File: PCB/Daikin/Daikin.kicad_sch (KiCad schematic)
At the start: 19 parts, among them J1 1x4, J2 Prog, Q3 PMF250XNEX, U1 ESP32-PICO-MINI-02, U2 LMR16006YDDCR

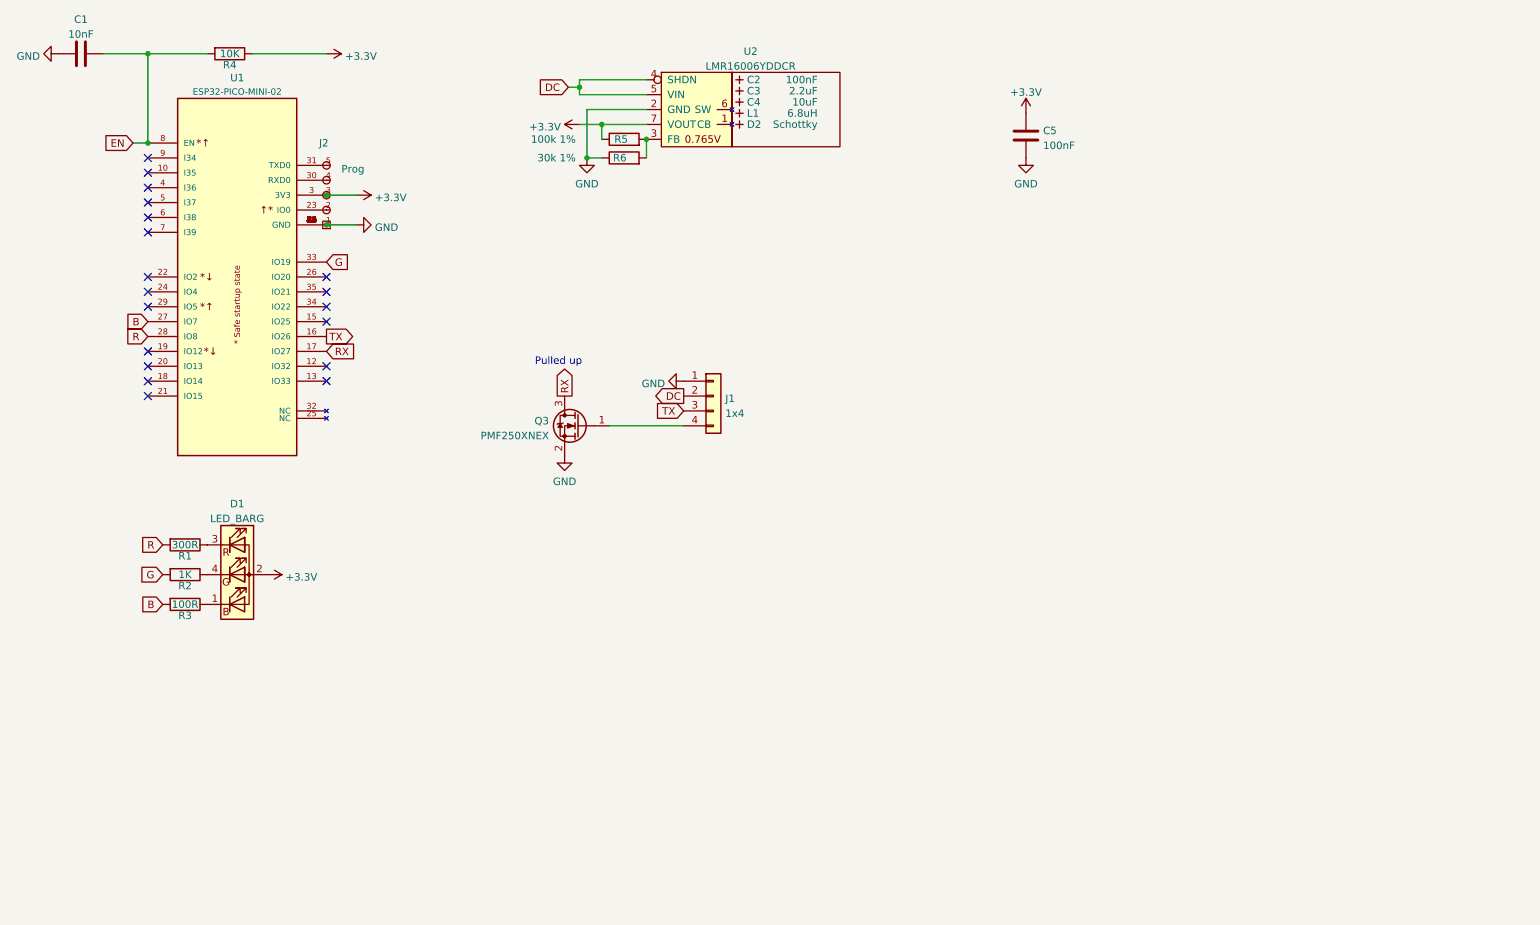
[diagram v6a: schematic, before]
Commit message: Changed PCB - larger so under pins making harder to fit plug the wrong way. Also changed to 5 pin connector to natch the actual plug to avoid confusion.
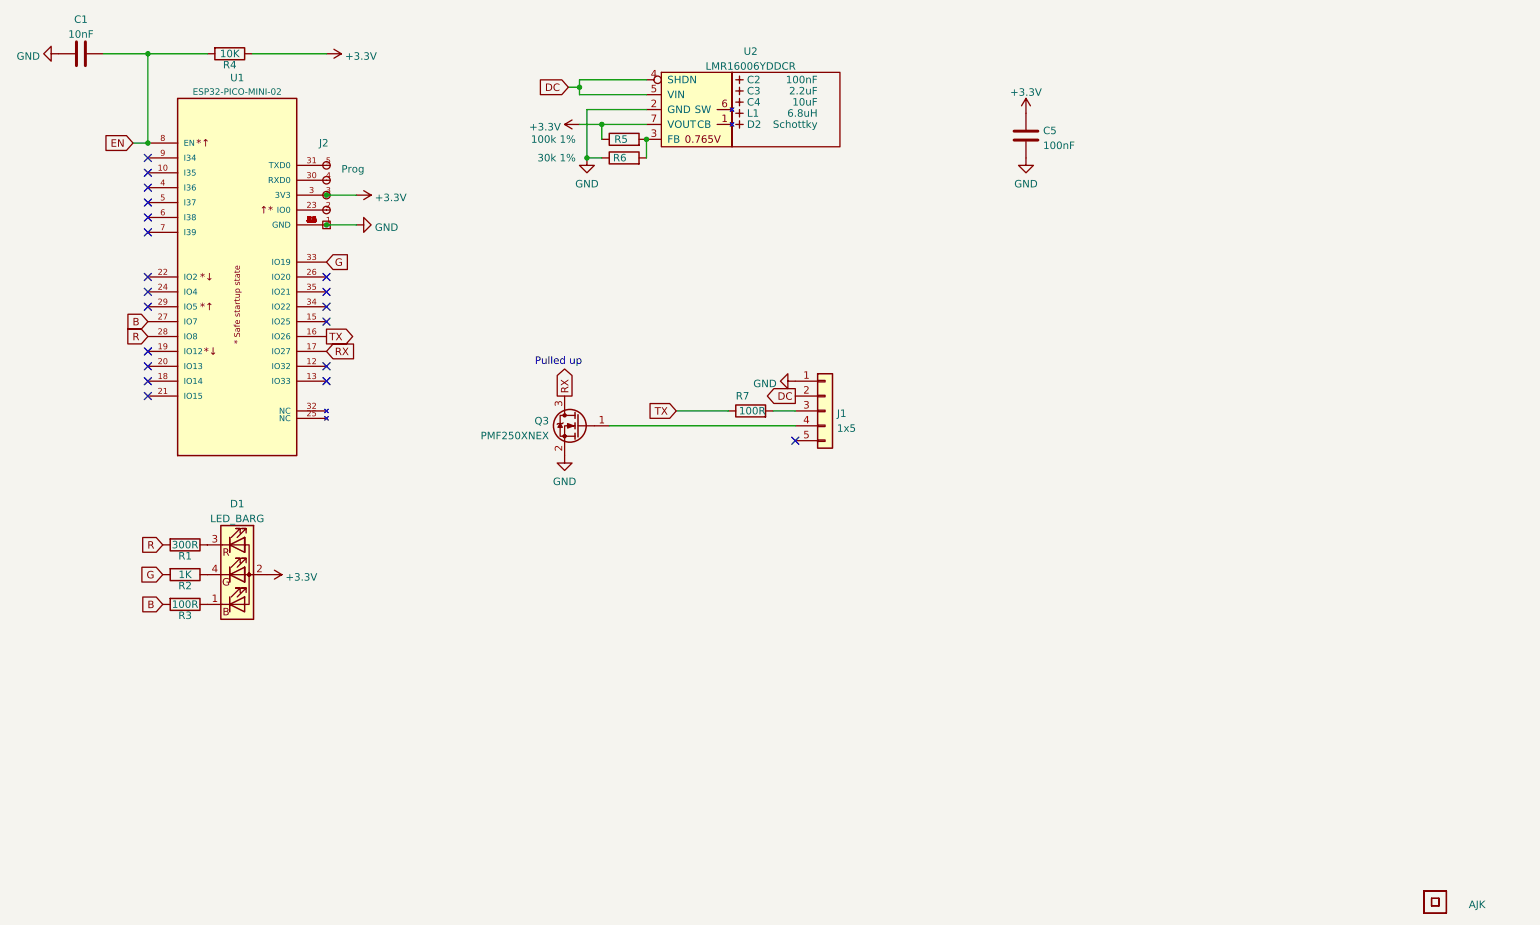
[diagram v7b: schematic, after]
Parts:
- added Logo1: AJK, RevK:AJK, symbol RevK:AJK
- added R7: 100R, RevK:R_0603, symbol Device:R
- added U3: QR, RevK:QR-DAIKIN, symbol RevK:QR
- J1: value 1x4 -> 1x5; footprint RevK:JLC-PinHeader_1x04_P2.54mm_Right -> RevK:PinHeader_1x05_P2.54mm_Right; symbol Connector_Generic:Conn_01x04 -> Connector_Generic:Conn_01x05; LCSC Part # C91552 -> C225491
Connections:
- net TX: now also R7.1; no longer J1.3 (Pin_3)
- new net: J1.3 (Pin_3), R7.2
- no-connect marks 19 -> 20
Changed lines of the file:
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@@
   (junction (at 81.28 57.15) (diameter 0) (color 0 0 0 0)
   )
+  (no_connect (at 161.29 93.98))
   (no_connect (at 81.28 71.12))
   (no_connect (at 50.8 45.72))
@@
     (stroke (width 0) (type default) (color 0 0 0 0))
   )
-  (wire (pts (xy 142.24 91.44) (xy 129.54 91.44))
+  (wire (pts (xy 161.29 91.44) (xy 129.54 91.44))
     (stroke (width 0) (type default) (color 0 0 0 0))
   )
@@
     (stroke (width 0) (type default) (color 0 0 0 0))
   )
+  (wire (pts (xy 140.97 88.9) (xy 149.86 88.9))
+    (stroke (width 0) (type default) (color 0 0 0 0))
+  )
   (wire (pts (xy 128.27 40.005) (xy 135.89 40.005))
     (stroke (width 0) (type default) (color 0 0 0 0))
@@
   )
   (wire (pts (xy 124.46 32.385) (xy 135.89 32.385))
+    (stroke (width 0) (type default) (color 0 0 0 0))
+  )
+  (wire (pts (xy 157.48 88.9) (xy 161.29 88.9))
     (stroke (width 0) (type default) (color 0 0 0 0))
   )
@@
     )
   )
-  (global_label "TX" (shape input) (at 142.24 88.9 180) (fields_autoplaced)
+  (global_label "TX" (shape input) (at 140.97 88.9 180) (fields_autoplaced)
     (effects (font (size 1.27 1.27)) (justify right))
-    (property "Intersheet References" "${INTERSHEET_REFS}" (id 0) (at 137.7387 88.8206 0)
+    (property "Intersheet References" "${INTERSHEET_REFS}" (id 0) (at 136.4687 88.8206 0)
       (effects (font (size 1.27 1.27)) (justify right) hide)
     )
@@
     )
   )
-  (global_label "DC" (shape output) (at 142.24 86.36 180) (fields_autoplaced)
+  (global_label "DC" (shape output) (at 161.29 86.36 180) (fields_autoplaced)
     (effects (font (size 1.27 1.27)) (justify right))
-    (property "Intersheet References" "${INTERSHEET_REFS}" (id 0) (at 137.3758 86.2806 0)
+    (property "Intersheet References" "${INTERSHEET_REFS}" (id 0) (at 156.4258 86.2806 0)
       (effects (font (size 1.27 1.27)) (justify right) hide)
     )
@@
     (pin "7")
   )
-  (symbol (lib_id "power:GND") (at 142.24 83.82 270) (unit 1)
-    (in_bom yes) (on_board yes) (fields_autoplaced)
-    (property "Reference" "#PWR09" (id 0) (at 135.89 83.82 0)
-      (effects (font (size 1.27 1.27)) hide)
-    )
-    (property "Value" "GND" (id 1) (at 139.0651 84.2538 90)
+  (symbol (lib_id "power:GND") (at 161.29 83.82 270) (unit 1)
+    (in_bom yes) (on_board yes) (fields_autoplaced)
+    (property "Reference" "#PWR09" (id 0) (at 154.94 83.82 0)
+      (effects (font (size 1.27 1.27)) hide)
+    )
+    (property "Value" "GND" (id 1) (at 158.1151 84.2538 90)
       (effects (font (size 1.27 1.27)) (justify right))
     )
-    (property "Footprint" "" (id 2) (at 142.24 83.82 0)
-      (effects (font (size 1.27 1.27)) hide)
-    )
-    (property "Datasheet" "" (id 3) (at 142.24 83.82 0)
+    (property "Footprint" "" (id 2) (at 161.29 83.82 0)
+      (effects (font (size 1.27 1.27)) hide)
+    )
+    (property "Datasheet" "" (id 3) (at 161.29 83.82 0)
       (effects (font (size 1.27 1.27)) hide)
     )
@@
     (pin "~")
   )
+  (symbol (lib_id "Device:R") (at 153.67 88.9 90) (unit 1)
+    (in_bom yes) (on_board yes)
+    (property "Reference" "R7" (id 0) (at 151.13 86.36 90)
+      (effects (font (size 1.27 1.27)) (justify right))
+    )
+    (property "Value" "100R" (id 1) (at 156.21 88.9 90)
+      (effects (font (size 1.27 1.27)) (justify left))
+    )
+    (property "Footprint" "RevK:R_0603" (id 2) (at 153.67 90.678 90)
+      (effects (font (size 1.27 1.27)) hide)
+    )
+    (property "Datasheet" "~" (id 3) (at 153.67 88.9 0)
+      (effects (font (size 1.27 1.27)) hide)
+    )
+    (property "LCSC Part #" "C105588" (id 4) (at 153.67 88.9 90)
+      (effects (font (size 1.27 1.27)) hide)
+    )
+    (pin "1")
+    (pin "2")
+  )
   (symbol (lib_id "Device:LED_BARG") (at 66.04 116.84 0) (unit 1)
     (in_bom yes) (on_board yes) (fields_autoplaced)
@@
     (pin "2")
   )
-  (symbol (lib_id "Connector_Generic:Conn_01x04") (at 147.32 86.36 0) (unit 1)
-    (in_bom yes) (on_board yes) (fields_autoplaced)
-    (property "Reference" "J1" (id 0) (at 149.352 86.7953 0)
-      (effects (font (size 1.27 1.27)) (justify left))
-    )
-    (property "Value" "1x4" (id 1) (at 149.352 89.3322 0)
-      (effects (font (size 1.27 1.27)) (justify left))
-    )
-    (property "Footprint" "RevK:JLC-PinHeader_1x04_P2.54mm_Right" (id 2) (at 148.59 93.98 0)
-      (effects (font (size 1.27 1.27)) hide)
-    )
-    (property "Datasheet" "~" (id 3) (at 147.32 86.36 0)
-      (effects (font (size 1.27 1.27)) hide)
-    )
-    (property "LCSC Part #" "C91552" (id 4) (at 147.32 86.36 0)
+  (symbol (lib_id "Connector_Generic:Conn_01x05") (at 166.37 88.9 0) (unit 1)
+    (in_bom yes) (on_board yes) (fields_autoplaced)
+    (property "Reference" "J1" (id 0) (at 168.402 89.3353 0)
+      (effects (font (size 1.27 1.27)) (justify left))
+    )
+    (property "Value" "1x5" (id 1) (at 168.402 91.8722 0)
+      (effects (font (size 1.27 1.27)) (justify left))
+    )
+    (property "Footprint" "RevK:PinHeader_1x05_P2.54mm_Right" (id 2) (at 166.37 88.9 0)
+      (effects (font (size 1.27 1.27)) hide)
+    )
+    (property "Datasheet" "~" (id 3) (at 166.37 88.9 0)
+      (effects (font (size 1.27 1.27)) hide)
+    )
+    (property "LCSC Part #" "C225491" (id 4) (at 166.37 88.9 0)
       (effects (font (size 1.27 1.27)) hide)
     )
@@
     (pin "3")
     (pin "4")
+    (pin "5")
   )
   (symbol (lib_id "power:+3.3V") (at 71.12 116.84 270) (unit 1)
@@
     (pin "1")
   )
+  (symbol (lib_id "RevK:QR") (at 270.51 172.72 0) (unit 1)
+    (in_bom no) (on_board yes) (fields_autoplaced)
+    (property "Reference" "U3" (id 0) (at 270.51 175.895 0)
+      (effects (font (size 1.27 1.27)) hide)
+    )
+    (property "Value" "QR" (id 1) (at 270.51 175.895 0)
+      (effects (font (size 1.27 1.27)) hide)
+    )
+    (property "Footprint" "RevK:QR-DAIKIN" (id 2) (at 269.875 173.355 0)
+      (effects (font (size 1.27 1.27)) hide)
+    )
+    (property "Datasheet" "" (id 3) (at 269.875 173.355 0)
+      (effects (font (size 1.27 1.27)) hide)
+    )
+    (property "Note" "Non part, PCB printed" (id 4) (at 270.51 172.72 0)
+      (effects (font (size 1.27 1.27)) hide)
+    )
+  )
   (symbol (lib_id "Device:R") (at 132.08 42.545 90) (unit 1)
     (in_bom yes) (on_board yes)
@@
     (pin "5")
   )
+  (symbol (lib_id "RevK:AJK") (at 275.59 172.72 0) (unit 1)
+    (in_bom no) (on_board yes) (fields_autoplaced)
+    (property "Reference" "Logo1" (id 0) (at 275.59 170.18 0)
+      (effects (font (size 1.27 1.27)) hide)
+    )
+    (property "Value" "AJK" (id 1) (at 276.225 173.1538 0)
+      (effects (font (size 1.27 1.27)) (justify left))
+    )
+    (property "Footprint" "RevK:AJK" (id 2) (at 275.59 175.26 0)
+      (effects (font (size 1.27 1.27)) hide)
+    )
+    (property "Datasheet" "" (id 3) (at 275.59 175.26 0)
+      (effects (font (size 1.27 1.27)) hide)
+    )
+    (property "Note" "Non part, PCB printed" (id 4) (at 275.59 172.72 0)
+      (effects (font (size 1.27 1.27)) hide)
+    )
+  )
   (sheet_instances
     (path "/" (page "1"))
@@
     )
     (path "/af073fa6-a783-40f2-9751-692984a62ffc"
-      (reference "J1") (unit 1) (value "1x4") (footprint "RevK:JLC-PinHeader_1x04_P2.54mm_Right")
+      (reference "J1") (unit 1) (value "1x5") (footprint "RevK:PinHeader_1x05_P2.54mm_Right")
     )
     (path "/ee567585-ddb7-4c4a-a692-94261f4c4bce"
@@
       (reference "L1") (unit 1) (value "6.8uH") (footprint "RevK:L_4x4_")
     )
+    (path "/f93331c2-c430-4421-8c6c-fa9ccbf3197e"
+      (reference "Logo1") (unit 1) (value "AJK") (footprint "RevK:AJK")
+    )
     (path "/ebcfdf36-110d-4f79-9de0-e4fcd76c1d6e"
       (reference "Q3") (unit 1) (value "PMF250XNEX") (footprint "RevK:SOT-323_SC-70")
@@
       (reference "R6") (unit 1) (value "30k 1%") (footprint "RevK:R_0603")
     )
+    (path "/a10dd132-8952-4c17-b7c1-5ab3a5e86621"
+      (reference "R7") (unit 1) (value "100R") (footprint "RevK:R_0603")
+    )
     (path "/7943a3d5-b195-4a57-b3e1-ee29355f1eeb"
       (reference "U1") (unit 1) (value "ESP32-PICO-MINI-02") (footprint "RevK:ESP32-PICO-MINI-02")
@@
       (reference "U2") (unit 1) (value "LMR16006YDDCR") (footprint "RevK:SOT-23-Thin-6-Reg")
     )
-  )
+    (path "/dd024a75-cbfd-4a06-88fc-e180db89ebee"
+      (reference "U3") (unit 1) (value "QR") (footprint "RevK:QR-DAIKIN")
+    )
+  )

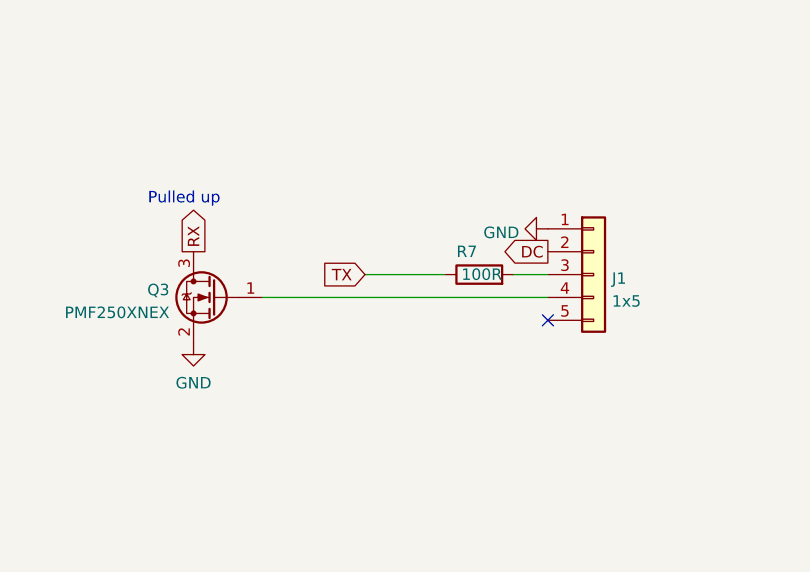
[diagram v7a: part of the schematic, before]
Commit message: Added some caps to I/O
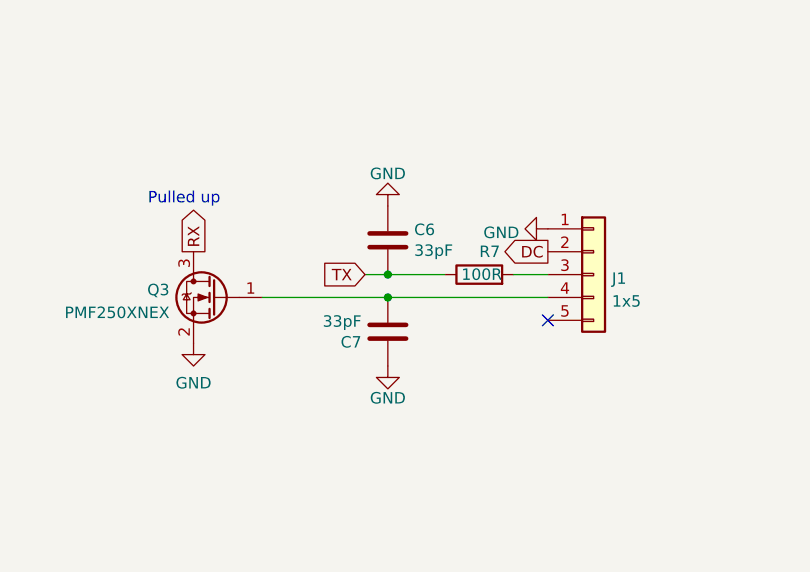
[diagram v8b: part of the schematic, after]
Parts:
- added C6, C7: 33pF, RevK:C_0603, symbol Device:C
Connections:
- net GND: now also C6.1, C7.1
- net TX: now also C6.2
- net at J1.4 (Pin_4), Q3.1 (G): now also C7.2
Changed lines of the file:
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@@
   (junction (at 128.27 40.005) (diameter 0) (color 0 0 0 0)
   )
+  (junction (at 143.51 91.44) (diameter 0) (color 0 0 0 0)
+  )
   (junction (at 81.28 52.07) (diameter 0) (color 0 0 0 0)
   )
   (junction (at 81.28 57.15) (diameter 0) (color 0 0 0 0)
+  )
+  (junction (at 143.51 88.9) (diameter 0) (color 0 0 0 0)
   )
   (no_connect (at 161.29 93.98))
@@
     (stroke (width 0) (type default) (color 0 0 0 0))
   )
-  (wire (pts (xy 161.29 91.44) (xy 129.54 91.44))
+  (wire (pts (xy 161.29 91.44) (xy 143.51 91.44))
     (stroke (width 0) (type default) (color 0 0 0 0))
   )
@@
     (stroke (width 0) (type default) (color 0 0 0 0))
   )
-  (wire (pts (xy 140.97 88.9) (xy 149.86 88.9))
+  (wire (pts (xy 140.97 88.9) (xy 143.51 88.9))
     (stroke (width 0) (type default) (color 0 0 0 0))
   )
@@
     (stroke (width 0) (type default) (color 0 0 0 0))
   )
+  (wire (pts (xy 143.51 91.44) (xy 129.54 91.44))
+    (stroke (width 0) (type default) (color 0 0 0 0))
+  )
   (wire (pts (xy 128.27 45.72) (xy 125.73 45.72))
     (stroke (width 0) (type default) (color 0 0 0 0))
@@
   )
   (wire (pts (xy 124.46 40.005) (xy 128.27 40.005))
+    (stroke (width 0) (type default) (color 0 0 0 0))
+  )
+  (wire (pts (xy 143.51 88.9) (xy 149.86 88.9))
     (stroke (width 0) (type default) (color 0 0 0 0))
   )
@@
     )
     (property "Part No" "0603-680R" (id 4) (at 57.15 111.76 90)
+      (effects (font (size 1.27 1.27)) hide)
+    )
+    (pin "1")
+    (pin "2")
+  )
+  (symbol (lib_id "Device:C") (at 143.51 95.25 180) (unit 1)
+    (in_bom yes) (on_board yes)
+    (property "Reference" "C7" (id 0) (at 140.589 96.4184 0)
+      (effects (font (size 1.27 1.27)) (justify left))
+    )
+    (property "Value" "33pF" (id 1) (at 140.589 94.107 0)
+      (effects (font (size 1.27 1.27)) (justify left))
+    )
+    (property "Footprint" "RevK:C_0603" (id 2) (at 142.5448 91.44 0)
+      (effects (font (size 1.27 1.27)) hide)
+    )
+    (property "Datasheet" "" (id 3) (at 143.51 95.25 0)
+      (effects (font (size 1.27 1.27)) hide)
+    )
+    (property "Note" "" (id 4) (at 143.51 95.25 0)
+      (effects (font (size 1.27 1.27)) hide)
+    )
+    (property "Part No" "0603-33pF-50V" (id 5) (at 143.51 95.25 0)
+      (effects (font (size 1.27 1.27)) hide)
+    )
+    (property "Manufacturer" "" (id 6) (at 143.51 95.25 0)
       (effects (font (size 1.27 1.27)) hide)
     )
@@
     (pin "~")
   )
+  (symbol (lib_id "Device:C") (at 143.51 85.09 0) (unit 1)
+    (in_bom yes) (on_board yes)
+    (property "Reference" "C6" (id 0) (at 146.431 83.9216 0)
+      (effects (font (size 1.27 1.27)) (justify left))
+    )
+    (property "Value" "33pF" (id 1) (at 146.431 86.233 0)
+      (effects (font (size 1.27 1.27)) (justify left))
+    )
+    (property "Footprint" "RevK:C_0603" (id 2) (at 144.4752 88.9 0)
+      (effects (font (size 1.27 1.27)) hide)
+    )
+    (property "Datasheet" "" (id 3) (at 143.51 85.09 0)
+      (effects (font (size 1.27 1.27)) hide)
+    )
+    (property "Note" "" (id 4) (at 143.51 85.09 0)
+      (effects (font (size 1.27 1.27)) hide)
+    )
+    (property "Part No" "0603-33pF-50V" (id 5) (at 143.51 85.09 0)
+      (effects (font (size 1.27 1.27)) hide)
+    )
+    (property "Manufacturer" "" (id 6) (at 143.51 85.09 0)
+      (effects (font (size 1.27 1.27)) hide)
+    )
+    (pin "1")
+    (pin "2")
+  )
   (symbol (lib_name "GND_1") (lib_id "power:GND") (at 86.36 57.15 90) (unit 1)
     (in_bom yes) (on_board yes) (fields_autoplaced)
@@
     )
     (property "Datasheet" "" (id 3) (at 86.36 57.15 0)
+      (effects (font (size 1.27 1.27)) hide)
+    )
+    (pin "1")
+  )
+  (symbol (lib_id "power:GND") (at 143.51 99.06 0) (unit 1)
+    (in_bom yes) (on_board yes) (fields_autoplaced)
+    (property "Reference" "#PWR0112" (id 0) (at 143.51 105.41 0)
+      (effects (font (size 1.27 1.27)) hide)
+    )
+    (property "Value" "GND" (id 1) (at 143.51 102.6358 0))
+    (property "Footprint" "" (id 2) (at 143.51 99.06 0)
+      (effects (font (size 1.27 1.27)) hide)
+    )
+    (property "Datasheet" "" (id 3) (at 143.51 99.06 0)
       (effects (font (size 1.27 1.27)) hide)
     )
@@
     (pin "1")
   )
+  (symbol (lib_id "power:GND") (at 143.51 81.28 180) (unit 1)
+    (in_bom yes) (on_board yes) (fields_autoplaced)
+    (property "Reference" "#PWR0111" (id 0) (at 143.51 74.93 0)
+      (effects (font (size 1.27 1.27)) hide)
+    )
+    (property "Value" "GND" (id 1) (at 143.51 77.7042 0))
+    (property "Footprint" "" (id 2) (at 143.51 81.28 0)
+      (effects (font (size 1.27 1.27)) hide)
+    )
+    (property "Datasheet" "" (id 3) (at 143.51 81.28 0)
+      (effects (font (size 1.27 1.27)) hide)
+    )
+    (pin "1")
+  )
   (symbol (lib_id "RevK:Hidden") (at 151.765 36.195 0) (unit 1)
     (in_bom yes) (on_board yes)
@@
   (symbol (lib_id "Device:R") (at 153.67 88.9 90) (unit 1)
     (in_bom yes) (on_board yes)
-    (property "Reference" "R7" (id 0) (at 151.13 86.36 90)
+    (property "Reference" "R7" (id 0) (at 153.67 86.36 90)
       (effects (font (size 1.27 1.27)) (justify right))
     )
@@
       (reference "#PWR0110") (unit 1) (value "GND") (footprint "")
     )
+    (path "/827028f1-95a2-4294-8547-b88883c41583"
+      (reference "#PWR0111") (unit 1) (value "GND") (footprint "")
+    )
+    (path "/635bd04e-4de8-4277-8a37-830ae7e5db3a"
+      (reference "#PWR0112") (unit 1) (value "GND") (footprint "")
+    )
     (path "/aea0762f-9b4b-49c8-b311-2b433e5a47c4"
       (reference "C1") (unit 1) (value "10nF") (footprint "RevK:C_0603")
@@
       (reference "C5") (unit 1) (value "100nF") (footprint "RevK:C_0603")
     )
+    (path "/41bcbb71-a469-46c7-8fec-73272ff186c2"
+      (reference "C6") (unit 1) (value "33pF") (footprint "RevK:C_0603")
+    )
+    (path "/0c7e21c9-b881-496b-ab3f-6197bafe47dd"
+      (reference "C7") (unit 1) (value "33pF") (footprint "RevK:C_0603")
+    )
     (path "/a7518107-ce5c-4f9d-bc2d-0e43ac670ca1"
